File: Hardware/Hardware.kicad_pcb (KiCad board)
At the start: 2 copper layers, 50 x 50 mm, 0 parts

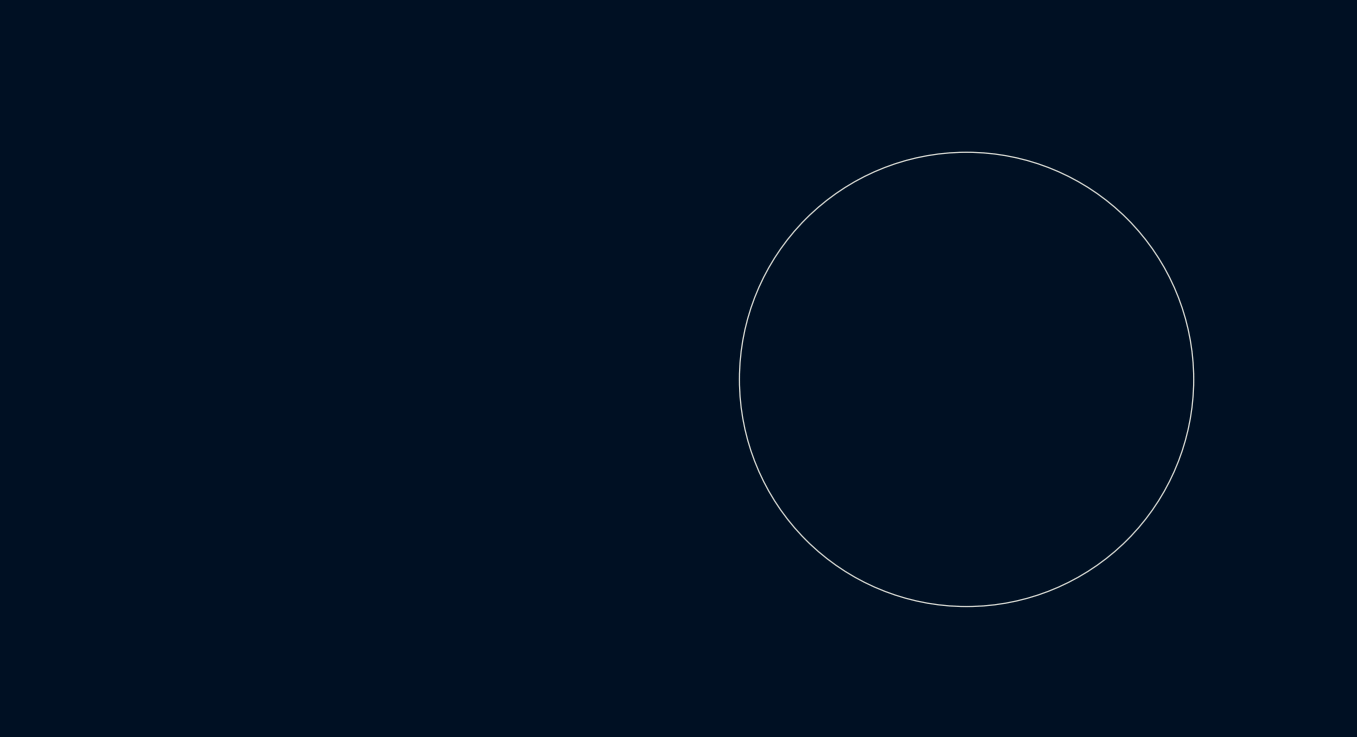
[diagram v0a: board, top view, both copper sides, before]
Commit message: feat: add components on schematic file
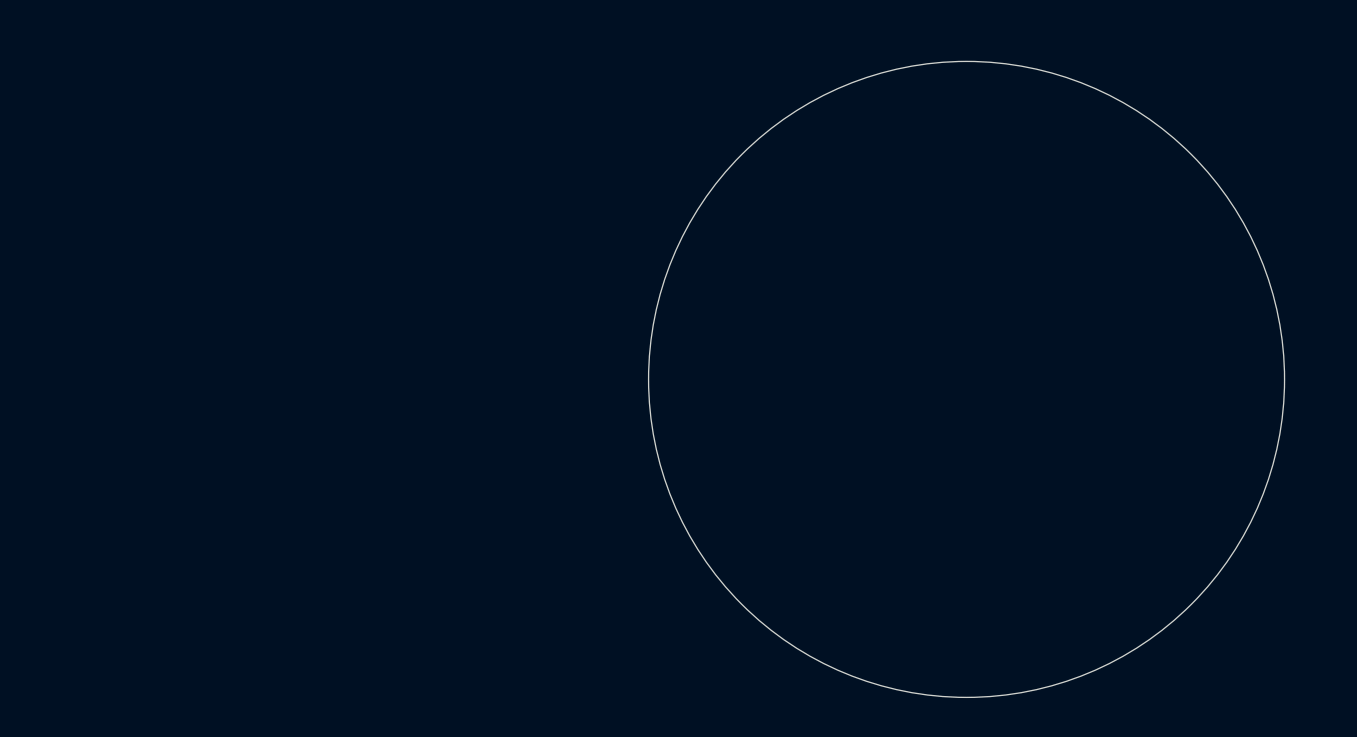
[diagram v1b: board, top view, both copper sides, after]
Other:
- board size 50 x 50 mm -> 70 x 70 mm
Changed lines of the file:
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@@
 	(gr_circle
 		(center 85.05 60.96)
-		(end 110.05 60.96)
+		(end 120.05 60.96)
 		(stroke
 			(width 0.05)
@@
 	)
 	(image
-		(at 85.05 60.960001)
+		(at 85.5 61.199395)
 		(layer "Edge.Cuts")
-		(scale 0.192571)
+		(scale 0.270465)
 		(data "/9j/4AAQSkZJRgABAQEASABIAAD/4gHYSUNDX1BST0ZJTEUAAQEAAAHIAAAAAAQwAABtbnRyUkdC"
 			"IFhZWiAH4AABAAEAAAAAAABhY3NwAAAAAAAAAAAAAAAAAAAAAAAAAAAAAAAAAAAAAQAA9tYAAQAA"

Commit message: feat: add components on pcb
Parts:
- added C10: 100nF, Capacitor_SMD:C_0805_2012Metric, B.Cu at (-11.6, 71.2)
- added C11: 100nF, Capacitor_SMD:C_0805_2012Metric, B.Cu at (102.0, 72.0)
- added C12: 100nF, Capacitor_SMD:C_0805_2012Metric, B.Cu at (112.0, 72.0)
- added C3: 100nF, Capacitor_SMD:C_0805_2012Metric, B.Cu at (-7.18, 65.2)
- added C4: 100nF, Capacitor_SMD:C_0805_2012Metric, B.Cu at (70.0, 75.5)
- added C5: 100nF, Capacitor_SMD:C_0805_2012Metric, B.Cu at (60.0, 75.5)
- added C6: 10uF, Capacitor_SMD:C_0805_2012Metric, B.Cu at (-7.18, 74.2)
- added C7: 100nF, Capacitor_SMD:C_0805_2012Metric, B.Cu at (-7.18, 77.2)
- added C8: 100nF, Capacitor_SMD:C_0805_2012Metric, B.Cu at (-11.6, 65.2)
- added C9: 100nF, Capacitor_SMD:C_0805_2012Metric, B.Cu at (-11.6, 68.2)
- added D1: LED, Connector_PinHeader_1.27mm:PinHeader_1x02_P1.27mm_Vertical, B.Cu at (116.2, 55.2)
- added D10: LED, LED_SMD:LED_0603_1608Metric, F.Cu at (83.0, 58.5)
- added D11: LED, LED_SMD:LED_0603_1608Metric, F.Cu at (76.5, 66.5)
- added D12: LED, LED_SMD:LED_0603_1608Metric, F.Cu at (86.0, 66.5)
- added D13: LED, LED_SMD:LED_0603_1608Metric, F.Cu at (97.2, 59.5)
- added D14: LED, LED_SMD:LED_0603_1608Metric, F.Cu at (65.0, 62.5)
- added D2: LED, Connector_PinHeader_1.27mm:PinHeader_1x02_P1.27mm_Vertical, B.Cu at (116.2, 59.4)
- added D3: LED, Connector_PinHeader_1.27mm:PinHeader_1x02_P1.27mm_Vertical, B.Cu at (116.2, 63.5)
- added D4: 1N5819, Diode_SMD:D_SOD-323, B.Cu at (-15.7, 77.2)
- added D5: LED, LED_SMD:LED_0603_1608Metric, F.Cu at (62.8, 50.5)
- added D6: LED, LED_SMD:LED_0603_1608Metric, F.Cu at (104.0, 47.5)
- added D7: LED, LED_SMD:LED_0603_1608Metric, F.Cu at (75.7, 46.0)
- added D8: LED, LED_SMD:LED_0603_1608Metric, F.Cu at (89.3, 44.5)
- added D9: LED, LED_SMD:LED_0603_1608Metric, F.Cu at (77.5, 57.0)
- added F1: Fuse_Small, Fuse:Fuse_0603_1608Metric, B.Cu at (77.5, 90.0)
- added J1: USB_C_Receptacle_USB2.0_16P, Connector_USB:USB_C_Receptacle_Palconn_UTC16-G, B.Cu at (85.2, 90.8)
- added J2: Conn_01x02_Socket, Connector_JST:JST_PH_S2B-PH-SM4-TB_1x02-1MP_P2.00mm_Horizontal, B.Cu at (60.1, 49.4)
- added J3: Conn_01x04_Pin, Connector_PinHeader_2.54mm:PinHeader_1x04_P2.54mm_Vertical, B.Cu at (113.0, 43.5)
- added Q1: AO3400A, Package_TO_SOT_SMD:SOT-23, B.Cu at (117.0, 67.0)
- added Q2: AO3401A, Package_TO_SOT_SMD:SOT-23, B.Cu at (63.5, 64.0)
- added R1: 33, Resistor_SMD:R_0805_2012Metric, B.Cu at (111.6, 56.6)
- added R10: 660, Resistor_SMD:R_0805_2012Metric, B.Cu at (-7.52, 56.3)
- added R11: 660, Resistor_SMD:R_0805_2012Metric, B.Cu at (-7.52, 59.3)
- added R12: 660, Resistor_SMD:R_0805_2012Metric, B.Cu at (-7.52, 62.2)
- added R13: 660, Resistor_SMD:R_0805_2012Metric, B.Cu at (-11.9, 47.5)
- added R14: 660, Resistor_SMD:R_0805_2012Metric, B.Cu at (-11.9, 50.4)
- added R15: 660, Resistor_SMD:R_0805_2012Metric, B.Cu at (-11.9, 53.4)
- added R16: 660, Resistor_SMD:R_0805_2012Metric, B.Cu at (-11.9, 56.3)
- added R17: 660, Resistor_SMD:R_0805_2012Metric, B.Cu at (-11.9, 59.3)
- added R18: 660, Resistor_SMD:R_0805_2012Metric, B.Cu at (-17.9, 65.0)
- added R19: 660, Resistor_SMD:R_0805_2012Metric, B.Cu at (-17.9, 68.0)
- added R2: 33, Resistor_SMD:R_0805_2012Metric, B.Cu at (111.6, 59.5)
- added R3: 33, Resistor_SMD:R_0805_2012Metric, B.Cu at (111.6, 62.5)
- added R4: 660, Resistor_SMD:R_0805_2012Metric, B.Cu at (112.0, 66.5)
- added R5: 660, Resistor_SMD:R_0805_2012Metric, B.Cu at (114.0, 66.5)
- added R6: 10k, Resistor_SMD:R_0805_2012Metric, B.Cu at (-3.11, 62.2)
- added R7: 660, Resistor_SMD:R_0805_2012Metric, B.Cu at (-7.52, 47.5)
- added R8: 5.1k, Resistor_SMD:R_0805_2012Metric, B.Cu at (88.0, 85.0)
- added R9: 5.1k, Resistor_SMD:R_0805_2012Metric, B.Cu at (82.5, 85.0)
- added SW2: ON, Button_Switch_SMD:SW_SPDT_Shouhan_MSK12C02, B.Cu at (53.0, 69.0)
- added U1: CH32V203CxTx, Package_QFP:LQFP-48_7x7mm_P0.5mm, B.Cu at (85.0, 75.0)
- added U2: AMS1117-3.3, Package_TO_SOT_SMD:SOT-223-3_TabPin2, B.Cu at (65.0, 75.0)
- added U3: TP4056-42-ESOP8, Package_SO:SOIC-8-1EP_3.9x4.9mm_P1.27mm_EP2.41x3.3mm_ThermalVias, B.Cu at (58.6, 58.8)
- added U4: AMS1117-3.3, Package_TO_SOT_SMD:SOT-223-3_TabPin2, B.Cu at (107.0, 69.7)
- added kibuzzard-6AC594A8: G***, kibuzzard-6AC594A8, B.Cu at (61.5, 49.0)
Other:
- outline, holes or cut-outs redrawn

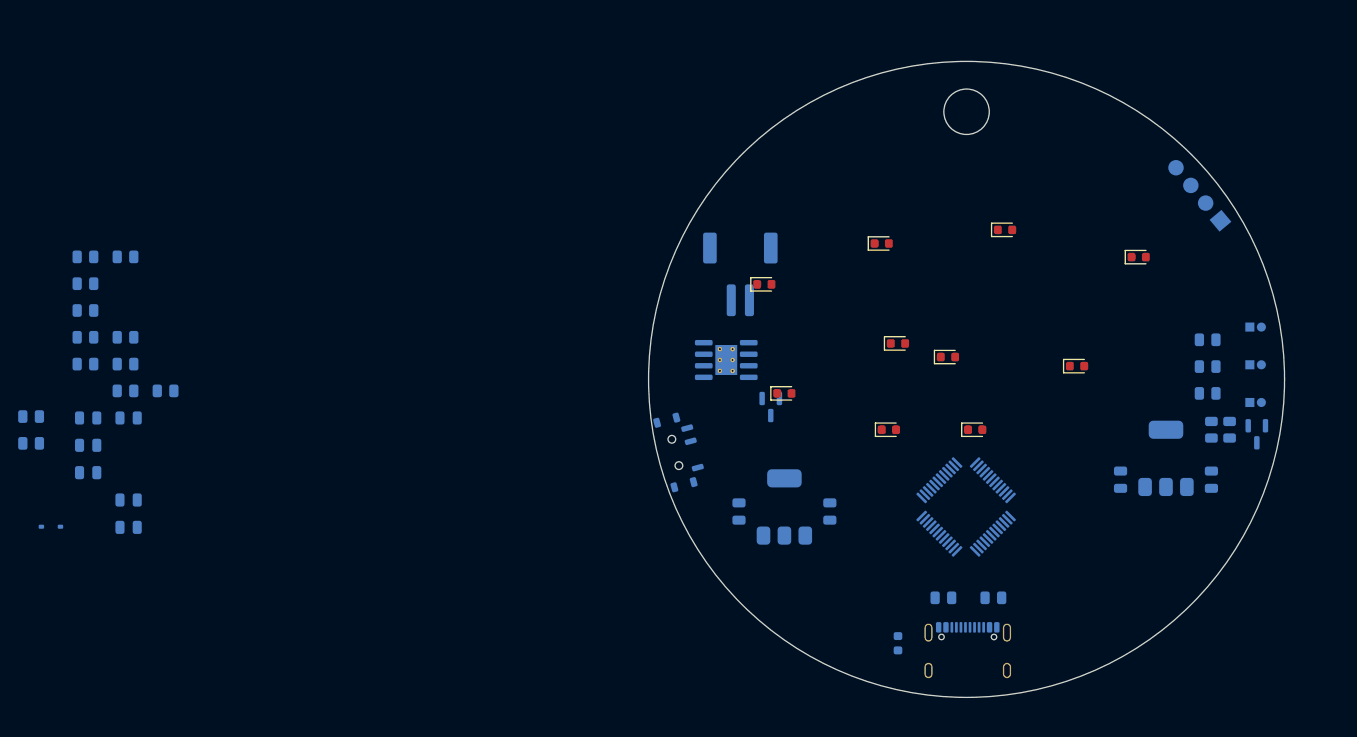
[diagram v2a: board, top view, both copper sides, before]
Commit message: feat: set component position
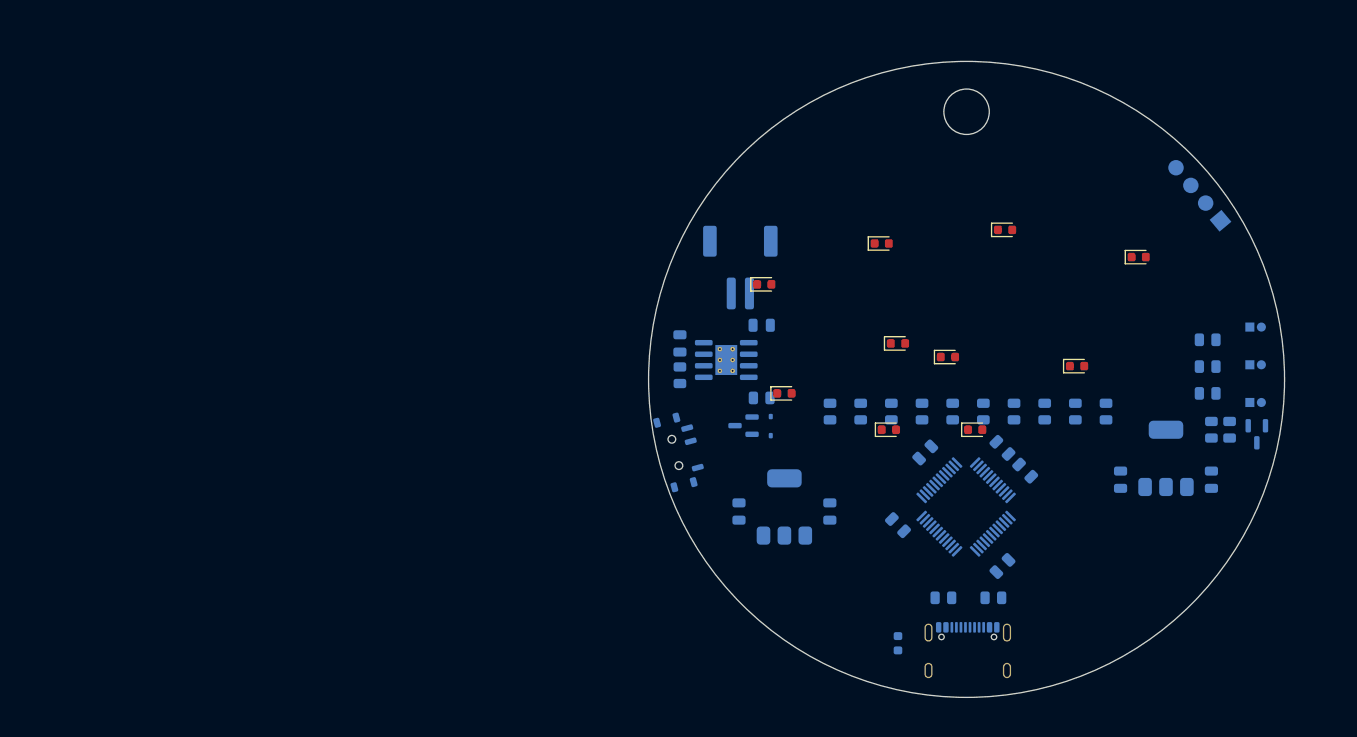
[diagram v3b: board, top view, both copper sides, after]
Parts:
- added C13: 10uF, Capacitor_SMD:C_0805_2012Metric, B.Cu at (53.5, 57.0)
- R4: value 660 -> 10
- R5: value 660 -> 10k
- R7: value 660 -> 1.2K
- moved R19 118.4 mm to (100.4, 64.5), turned to -90 degrees
- moved R18 114.9 mm to (97.0, 64.5), turned to -90 degrees
- moved R17 105.7 mm to (93.6, 64.5), turned to -90 degrees
- moved R16 102.5 mm to (90.3, 64.5), turned to -90 degrees
- moved C10 101.2 mm to (89.0, 81.5), turned to -135 degrees
- moved R15 99.5 mm to (86.9, 64.5), turned to -90 degrees
- moved C7 98.9 mm to (91.5, 71.0), turned to -45 degrees
- moved R14 96.5 mm to (83.5, 64.5), turned to -90 degrees
- moved C3 96.2 mm to (89.0, 68.5), turned to 135 degrees
- moved R13 93.6 mm to (80.1, 64.5), turned to -90 degrees
- moved C9 92.1 mm to (80.5, 69.0), turned to 45 degrees
- moved C8 89.9 mm to (77.5, 77.0), turned to -45 degrees
- moved R12 84.3 mm to (76.8, 64.5), turned to -90 degrees
- moved R11 81.1 mm to (73.4, 64.5), turned to -90 degrees
- moved D4 80.0 mm to (63.5, 66.1), turned to 90 degrees
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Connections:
- SW2 pad 2: Net-(D4-K) -> /OUT
- SW2 pad 3: /OUT -> Net-(D4-K)

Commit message: feat: add image
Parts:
- moved D5 9.94 mm to (65.7, 41.0)
- moved D14 4.08 mm to (65.8, 58.5)
- moved D10 3.16 mm to (84.0, 61.5)
- moved R1 3.11 mm to (108.9, 55.1)
- moved R2 3.11 mm to (108.9, 58.0)
- moved R3 3.11 mm to (108.9, 61.0)
- moved D9 3.04 mm to (77.0, 60.0)
- moved J3 2.76 mm to (110.8, 45.2)
- moved C11 1.85 mm to (100.2, 72.0)
- moved C12 1.85 mm to (110.2, 72.0)
- moved Q1 1.85 mm to (115.2, 67.0)
- moved R4 1.85 mm to (110.2, 66.5)
- moved R5 1.85 mm to (112.2, 66.5)
- moved U4 1.85 mm to (105.2, 69.7)
- moved D1 1.74 mm to (115.4, 53.7)
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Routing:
- net /D+: track 0.00 -> 18.3 mm
- net /D-: track 0.00 -> 17.5 mm
- net GND: track 0.00 -> 6.67 mm
- net Net-(J1-CC1): track 0.00 -> 3.52 mm
- net Net-(J1-CC2): track 0.00 -> 3.26 mm
- added copper zone on B.Cu, net GND
- added copper zone on F.Cu, net GND

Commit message: feat: add some routes
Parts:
- moved J1 25.1 mm to (62.4, 80.4), turned to 130 degrees
- moved F1 24.9 mm to (58.4, 74.0), turned to 40 degrees
- moved R8 21.1 mm to (68.0, 78.5), turned to -50 degrees
- moved R9 20.3 mm to (64.9, 74.9), turned to 130 degrees
- moved C5 10.2 mm to (68.8, 70.3)
- moved U2 9.28 mm to (73.8, 71.9)
- moved C12 7.75 mm to (104.9, 66.3), turned to 180 degrees
- moved C10 7.33 mm to (89.0, 88.8)
- moved C3 7.33 mm to (89.0, 75.8)
- moved C7 7.33 mm to (91.5, 78.3)
- moved C8 7.33 mm to (77.5, 84.3)
- moved C9 7.33 mm to (80.5, 76.3)
- moved U1 7.33 mm to (85.0, 82.3)
- moved C4 5.39 mm to (75.0, 77.5), turned to 180 degrees
- moved C11 3.08 mm to (98.1, 74.3)
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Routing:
- net /OUT: track 0.00 -> 77.1 mm, vias 0 -> 2
- net +3.3V: track 0.00 -> 52.5 mm
- net +5V: track 0.00 -> 26.3 mm, vias 0 -> 2
- net /D-: track 17.5 -> 34.9 mm, vias 0 -> 2
- net /D+: track 18.3 -> 34.8 mm, vias 0 -> 2
- net Net-(U1-VBAT): track 0.00 -> 3.28 mm
- net Net-(U3-PROG): track 0.00 -> 2.68 mm
- net GND: track 6.67 -> 6.25 mm, vias 0 -> 5
- added copper zone on B.Cu, net +5V
- added copper zone on B.Cu, net +BATT

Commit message: feat: add routes
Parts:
- added R20: 10k, Resistor_SMD:R_0805_2012Metric, B.Cu at (96.8, 80.2)
- added R21: 10k, Resistor_SMD:R_0805_2012Metric, B.Cu at (100.8, 80.2)
- added SW1: SW_Push, Button_Switch_SMD:SW_SPST_PTS810, B.Cu at (96.8, 84.4)
- added SW3: SW_Push, Button_Switch_SMD:SW_SPST_PTS810, B.Cu at (100.8, 84.5)
- moved J3 58.7 mm to (75.3, 92.1), turned to 60 degrees
- moved D13 37.3 mm to (65.7, 41.0)
- moved D5 37.2 mm to (97.7, 60.0)
- moved R19 30.4 mm to (70.0, 63.6)
- moved R10 30.3 mm to (100.4, 63.6)
- moved R18 23.7 mm to (73.3, 63.6)
- moved R11 23.6 mm to (97.0, 63.6)
- moved D11 22.0 mm to (75.7, 46.0)
- moved D8 17.8 mm to (84.0, 61.5)
- moved R17 17.0 mm to (76.7, 63.6)
- moved R12 16.9 mm to (93.6, 63.6)
- moved D7 13.7 mm to (89.3, 44.5)
- moved D9 11.2 mm to (85.3, 67.5)
- moved D12 11.2 mm to (77.0, 60.0)
- moved D10 10.3 mm to (76.0, 68.0)
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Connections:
- U1 pad 10: unconnected-(U1-PA0-Pad10) -> /control
- U1 pad 18: /LED_1 -> unconnected-(U1-PB0-Pad18)
- U1 pad 19: /LED_2 -> unconnected-(U1-PB1-Pad19)
- U1 pad 2: unconnected-(U1-PC13-Pad2) -> /LED_3
- U1 pad 20: /LED_3 -> unconnected-(U1-PB2-Pad20)
- U1 pad 21: /control -> unconnected-(U1-PB10-Pad21)
- U1 pad 3: unconnected-(U1-PC14-Pad3) -> /LED_2
- U1 pad 39: /LED_4 -> /LED_10
- U1 pad 4: unconnected-(U1-PC15-Pad4) -> /LED_1
- U1 pad 40: /LED_5 -> /LED_9
- U1 pad 41: /LED_6 -> /LED_8
- U1 pad 43: /LED_8 -> /LED_6
- U1 pad 45: /LED_9 -> /LED_5
- U1 pad 46: /LED_10 -> /LED_4
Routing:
- net /OUT: track 77.1 -> 26.7 mm, vias 2 -> 0
- net +3.3V: track 52.5 -> 93.8 mm
- net Net-(F1-Pad1): track 0.00 -> 31.9 mm
- net Net-(D13-A): track 0.00 -> 27.9 mm, vias 0 -> 1
- net /BOOT0: track 0.00 -> 27.4 mm, vias 0 -> 2
- net /LED_1: track 0.00 -> 26.3 mm, vias 0 -> 2
- net /LED_10: track 0.00 -> 25.4 mm, vias 0 -> 2
- net +3V3: track 0.00 -> 23.3 mm
- net /LED_2: track 0.00 -> 22.7 mm, vias 0 -> 2
- net /LED_9: track 0.00 -> 21.8 mm, vias 0 -> 2
- net /NRESET: track 0.00 -> 21.3 mm, vias 0 -> 2
- net Net-(D7-A): track 0.00 -> 21.2 mm, vias 0 -> 1
- net /LED_4: track 0.00 -> 20.7 mm, vias 0 -> 2
- net /LED_3: track 0.00 -> 19.1 mm, vias 0 -> 2
- net /LED_5: track 0.00 -> 18.9 mm, vias 0 -> 2
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
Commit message: feat: add routes
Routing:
- net /OUT: track 26.7 -> 59.7 mm, vias 0 -> 2
- net /control: track 1.49 -> 33.2 mm, vias 1 -> 2
- net Net-(D6-A): track 0.00 -> 25.3 mm, vias 0 -> 1
- net Net-(D11-A): track 0.00 -> 19.8 mm, vias 0 -> 1

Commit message: feat: finish routes
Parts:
- D1, D2, D3: footprint Connector_PinHeader_1.27mm:PinHeader_1x02_P1.27mm_Vertical -> Connector_PinHeader_2.54mm:PinHeader_1x02_P2.54mm_Vertical
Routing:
- net GND: track 10.2 -> 12.9 mm
- net Net-(D1-A): track 6.48 -> 4.70 mm
- net Net-(D3-A): track 6.34 -> 4.62 mm
- net Net-(D2-A): track 5.48 -> 4.34 mm
